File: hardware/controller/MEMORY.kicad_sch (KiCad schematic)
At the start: 8 parts, among them IC3 4677, IC4 W25Q256JVEIQ

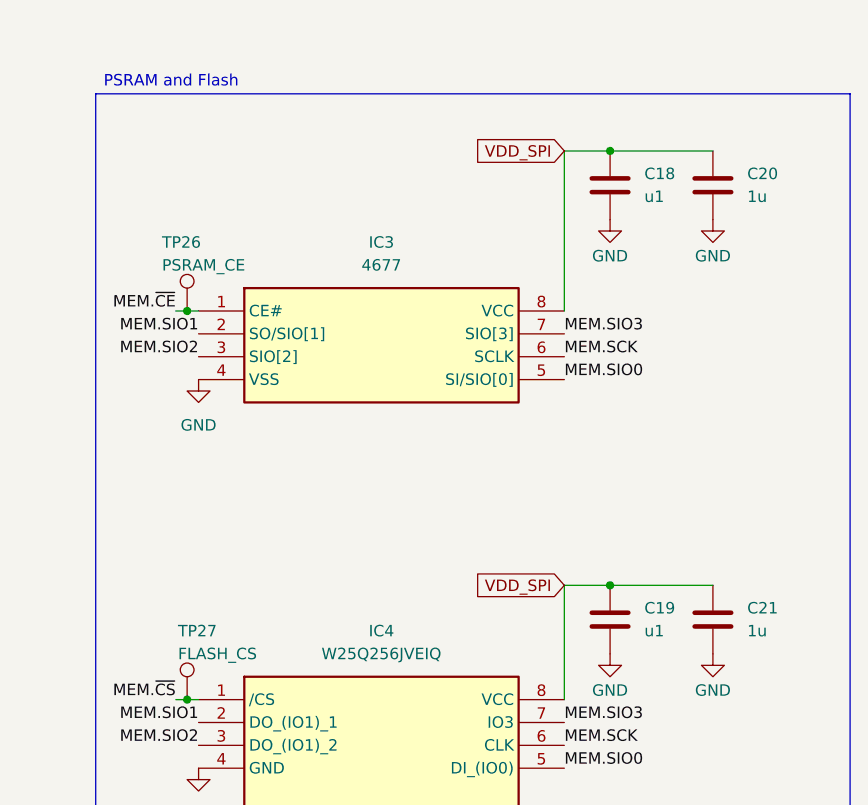
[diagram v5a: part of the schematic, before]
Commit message: ERC good to go. grouped all components on pcb
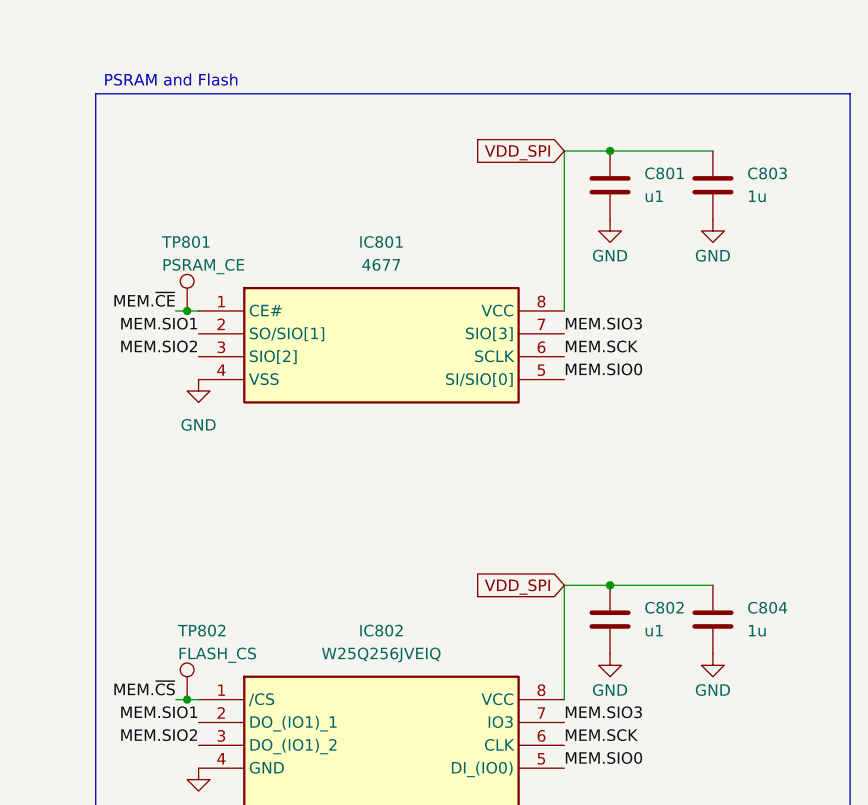
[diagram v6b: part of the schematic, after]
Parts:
- C801: renamed from C18; footprint MAJx16 -> SamacSys_Parts:MAJx16
- C802: renamed from C19; footprint MAJx16 -> SamacSys_Parts:MAJx16
- C803: renamed from C20; footprint CAPC2012X135N -> SamacSys_Parts:CAPC2012X135N
- C804: renamed from C21; footprint CAPC2012X135N -> SamacSys_Parts:CAPC2012X135N
- IC801: renamed from IC3; footprint SOIC127P600X175-8N -> SamacSys_Parts:SOIC127P600X175-8N
- IC802: renamed from IC4; footprint SON127P800X600X80-9N-D -> SamacSys_Parts:SON127P800X600X80-9N-D
- renumbered TP26 to TP801, TP27 to TP802
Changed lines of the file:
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@@
 		(dnp no)
 		(fields_autoplaced yes)
-		(property "Reference" "#PWR062"
+		(property "Reference" "#PWR0801"
 			(at 119.38 96.52 0)
 			(effects
@@
 			(project "controller"
 				(path "/869bea87-c885-4ead-826b-3f34ceacafad/0e7b3f4d-646f-4949-ba8d-4e4489aa7d1d"
-					(reference "#PWR062")
+					(reference "#PWR0801")
 					(unit 1)
 				)
@@
 		(dnp no)
 		(fields_autoplaced yes)
-		(property "Reference" "C19"
+		(property "Reference" "C802"
 			(at 168.91 115.5699 0)
 			(effects
@@
 			)
 		)
-		(property "Footprint" "MAJx16"
+		(property "Footprint" "SamacSys_Parts:MAJx16"
 			(at 173.99 213.03 0)
 			(effects
@@
 			(project "controller"
 				(path "/869bea87-c885-4ead-826b-3f34ceacafad/0e7b3f4d-646f-4949-ba8d-4e4489aa7d1d"
-					(reference "C19")
+					(reference "C802")
 					(unit 1)
 				)
@@
 		(dnp no)
 		(fields_autoplaced yes)
-		(property "Reference" "IC4"
+		(property "Reference" "IC802"
 			(at 139.7 118.11 0)
 			(effects
@@
 			)
 		)
-		(property "Footprint" "SON127P800X600X80-9N-D"
+		(property "Footprint" "SamacSys_Parts:SON127P800X600X80-9N-D"
 			(at 156.21 220.65 0)
 			(effects
@@
 			(project "controller"
 				(path "/869bea87-c885-4ead-826b-3f34ceacafad/0e7b3f4d-646f-4949-ba8d-4e4489aa7d1d"
-					(reference "IC4")
+					(reference "IC802")
 					(unit 1)
 				)
@@
 		(on_board yes)
 		(dnp no)
-		(property "Reference" "#PWR067"
+		(property "Reference" "#PWR0806"
 			(at 176.53 78.74 0)
 			(effects
@@
 			(project "controller"
 				(path "/869bea87-c885-4ead-826b-3f34ceacafad/0e7b3f4d-646f-4949-ba8d-4e4489aa7d1d"
-					(reference "#PWR067")
+					(reference "#PWR0806")
 					(unit 1)
 				)
@@
 		(dnp no)
 		(fields_autoplaced yes)
-		(property "Reference" "C20"
+		(property "Reference" "C803"
 			(at 180.34 67.3099 0)
 			(effects
@@
 			)
 		)
-		(property "Footprint" "CAPC2012X135N"
+		(property "Footprint" "SamacSys_Parts:CAPC2012X135N"
 			(at 185.42 164.77 0)
 			(effects
@@
 			(project "controller"
 				(path "/869bea87-c885-4ead-826b-3f34ceacafad/0e7b3f4d-646f-4949-ba8d-4e4489aa7d1d"
-					(reference "C20")
+					(reference "C803")
 					(unit 1)
 				)
@@
 		(dnp no)
 		(fields_autoplaced yes)
-		(property "Reference" "IC3"
+		(property "Reference" "IC801"
 			(at 139.7 74.93 0)
 			(effects
@@
 			)
 		)
-		(property "Footprint" "SOIC127P600X175-8N"
+		(property "Footprint" "SamacSys_Parts:SOIC127P600X175-8N"
 			(at 156.21 177.47 0)
 			(effects
@@
 			(project "controller"
 				(path "/869bea87-c885-4ead-826b-3f34ceacafad/0e7b3f4d-646f-4949-ba8d-4e4489aa7d1d"
-					(reference "IC3")
+					(reference "IC801")
 					(unit 1)
 				)
@@
 		(on_board yes)
 		(dnp no)
-		(property "Reference" "#PWR065"
+		(property "Reference" "#PWR0804"
 			(at 165.1 78.74 0)
 			(effects
@@
 			(project "controller"
 				(path "/869bea87-c885-4ead-826b-3f34ceacafad/0e7b3f4d-646f-4949-ba8d-4e4489aa7d1d"
-					(reference "#PWR065")
+					(reference "#PWR0804")
 					(unit 1)
 				)
@@
 		(dnp no)
 		(fields_autoplaced yes)
-		(property "Reference" "#PWR064"
+		(property "Reference" "#PWR0803"
 			(at 139.7 152.4 0)
 			(effects
@@
 			(project "controller"
 				(path "/869bea87-c885-4ead-826b-3f34ceacafad/0e7b3f4d-646f-4949-ba8d-4e4489aa7d1d"
-					(reference "#PWR064")
+					(reference "#PWR0803")
 					(unit 1)
 				)
@@
 		(on_board yes)
 		(dnp no)
-		(property "Reference" "#PWR068"
+		(property "Reference" "#PWR0807"
 			(at 176.53 127 0)
 			(effects
@@
 			(project "controller"
 				(path "/869bea87-c885-4ead-826b-3f34ceacafad/0e7b3f4d-646f-4949-ba8d-4e4489aa7d1d"
-					(reference "#PWR068")
+					(reference "#PWR0807")
 					(unit 1)
 				)
@@
 		(on_board yes)
 		(dnp no)
-		(property "Reference" "#PWR066"
+		(property "Reference" "#PWR0805"
 			(at 165.1 127 0)
 			(effects
@@
 			(project "controller"
 				(path "/869bea87-c885-4ead-826b-3f34ceacafad/0e7b3f4d-646f-4949-ba8d-4e4489aa7d1d"
-					(reference "#PWR066")
+					(reference "#PWR0805")
 					(unit 1)
 				)
@@
 		(on_board yes)
 		(dnp no)
-		(property "Reference" "TP27"
+		(property "Reference" "TP802"
 			(at 117.094 118.11 0)
 			(effects
@@
 			(project "controller"
 				(path "/869bea87-c885-4ead-826b-3f34ceacafad/0e7b3f4d-646f-4949-ba8d-4e4489aa7d1d"
-					(reference "TP27")
+					(reference "TP802")
 					(unit 1)
 				)
@@
 		(dnp no)
 		(fields_autoplaced yes)
-		(property "Reference" "#PWR063"
+		(property "Reference" "#PWR0802"
 			(at 119.38 139.7 0)
 			(effects
@@
 			(project "controller"
 				(path "/869bea87-c885-4ead-826b-3f34ceacafad/0e7b3f4d-646f-4949-ba8d-4e4489aa7d1d"
-					(reference "#PWR063")
+					(reference "#PWR0802")
 					(unit 1)
 				)
@@
 		(dnp no)
 		(fields_autoplaced yes)
-		(property "Reference" "C18"
+		(property "Reference" "C801"
 			(at 168.91 67.3099 0)
 			(effects
@@
 			)
 		)
-		(property "Footprint" "MAJx16"
+		(property "Footprint" "SamacSys_Parts:MAJx16"
 			(at 173.99 164.77 0)
 			(effects
@@
 			(project "controller"
 				(path "/869bea87-c885-4ead-826b-3f34ceacafad/0e7b3f4d-646f-4949-ba8d-4e4489aa7d1d"
-					(reference "C18")
+					(reference "C801")
 					(unit 1)
 				)
@@
 		(on_board yes)
 		(dnp no)
-		(property "Reference" "TP26"
+		(property "Reference" "TP801"
 			(at 115.316 74.93 0)
 			(effects
@@
 			(project "controller"
 				(path "/869bea87-c885-4ead-826b-3f34ceacafad/0e7b3f4d-646f-4949-ba8d-4e4489aa7d1d"
-					(reference "TP26")
+					(reference "TP801")
 					(unit 1)
 				)
@@
 		(dnp no)
 		(fields_autoplaced yes)
-		(property "Reference" "C21"
+		(property "Reference" "C804"
 			(at 180.34 115.5699 0)
 			(effects
@@
 			)
 		)
-		(property "Footprint" "CAPC2012X135N"
+		(property "Footprint" "SamacSys_Parts:CAPC2012X135N"
 			(at 185.42 213.03 0)
 			(effects
@@
 			(project "controller"
 				(path "/869bea87-c885-4ead-826b-3f34ceacafad/0e7b3f4d-646f-4949-ba8d-4e4489aa7d1d"
-					(reference "C21")
-					(unit 1)
-				)
+					(reference "C804")
+					(unit 1)
+				)

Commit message: save before nuke
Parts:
- renumbered C801 to C119, C802 to C120, C803 to C121, C804 to C122, IC801 to IC103, IC802 to IC104, TP801 to TP126, TP802 to TP127
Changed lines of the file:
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@@
 		(dnp no)
 		(fields_autoplaced yes)
-		(property "Reference" "#PWR0801"
+		(property "Reference" "#PWR0163"
 			(at 119.38 96.52 0)
 			(effects
@@
 			(project "controller"
 				(path "/869bea87-c885-4ead-826b-3f34ceacafad/0e7b3f4d-646f-4949-ba8d-4e4489aa7d1d"
-					(reference "#PWR0801")
+					(reference "#PWR0163")
 					(unit 1)
 				)
@@
 		(dnp no)
 		(fields_autoplaced yes)
-		(property "Reference" "C802"
+		(property "Reference" "C120"
 			(at 168.91 115.5699 0)
 			(effects
@@
 			(project "controller"
 				(path "/869bea87-c885-4ead-826b-3f34ceacafad/0e7b3f4d-646f-4949-ba8d-4e4489aa7d1d"
-					(reference "C802")
+					(reference "C120")
 					(unit 1)
 				)
@@
 		(dnp no)
 		(fields_autoplaced yes)
-		(property "Reference" "IC802"
+		(property "Reference" "IC104"
 			(at 139.7 118.11 0)
 			(effects
@@
 			(project "controller"
 				(path "/869bea87-c885-4ead-826b-3f34ceacafad/0e7b3f4d-646f-4949-ba8d-4e4489aa7d1d"
-					(reference "IC802")
+					(reference "IC104")
 					(unit 1)
 				)
@@
 		(on_board yes)
 		(dnp no)
-		(property "Reference" "#PWR0806"
+		(property "Reference" "#PWR0168"
 			(at 176.53 78.74 0)
 			(effects
@@
 			(project "controller"
 				(path "/869bea87-c885-4ead-826b-3f34ceacafad/0e7b3f4d-646f-4949-ba8d-4e4489aa7d1d"
-					(reference "#PWR0806")
+					(reference "#PWR0168")
 					(unit 1)
 				)
@@
 		(dnp no)
 		(fields_autoplaced yes)
-		(property "Reference" "C803"
+		(property "Reference" "C121"
 			(at 180.34 67.3099 0)
 			(effects
@@
 			(project "controller"
 				(path "/869bea87-c885-4ead-826b-3f34ceacafad/0e7b3f4d-646f-4949-ba8d-4e4489aa7d1d"
-					(reference "C803")
+					(reference "C121")
 					(unit 1)
 				)
@@
 		(dnp no)
 		(fields_autoplaced yes)
-		(property "Reference" "IC801"
+		(property "Reference" "IC103"
 			(at 139.7 74.93 0)
 			(effects
@@
 			(project "controller"
 				(path "/869bea87-c885-4ead-826b-3f34ceacafad/0e7b3f4d-646f-4949-ba8d-4e4489aa7d1d"
-					(reference "IC801")
+					(reference "IC103")
 					(unit 1)
 				)
@@
 		(on_board yes)
 		(dnp no)
-		(property "Reference" "#PWR0804"
+		(property "Reference" "#PWR0166"
 			(at 165.1 78.74 0)
 			(effects
@@
 			(project "controller"
 				(path "/869bea87-c885-4ead-826b-3f34ceacafad/0e7b3f4d-646f-4949-ba8d-4e4489aa7d1d"
-					(reference "#PWR0804")
+					(reference "#PWR0166")
 					(unit 1)
 				)
@@
 		(dnp no)
 		(fields_autoplaced yes)
-		(property "Reference" "#PWR0803"
+		(property "Reference" "#PWR0165"
 			(at 139.7 152.4 0)
 			(effects
@@
 			(project "controller"
 				(path "/869bea87-c885-4ead-826b-3f34ceacafad/0e7b3f4d-646f-4949-ba8d-4e4489aa7d1d"
-					(reference "#PWR0803")
+					(reference "#PWR0165")
 					(unit 1)
 				)
@@
 		(on_board yes)
 		(dnp no)
-		(property "Reference" "#PWR0807"
+		(property "Reference" "#PWR0169"
 			(at 176.53 127 0)
 			(effects
@@
 			(project "controller"
 				(path "/869bea87-c885-4ead-826b-3f34ceacafad/0e7b3f4d-646f-4949-ba8d-4e4489aa7d1d"
-					(reference "#PWR0807")
+					(reference "#PWR0169")
 					(unit 1)
 				)
@@
 		(on_board yes)
 		(dnp no)
-		(property "Reference" "#PWR0805"
+		(property "Reference" "#PWR0167"
 			(at 165.1 127 0)
 			(effects
@@
 			(project "controller"
 				(path "/869bea87-c885-4ead-826b-3f34ceacafad/0e7b3f4d-646f-4949-ba8d-4e4489aa7d1d"
-					(reference "#PWR0805")
+					(reference "#PWR0167")
 					(unit 1)
 				)
@@
 		(on_board yes)
 		(dnp no)
-		(property "Reference" "TP802"
+		(property "Reference" "TP127"
 			(at 117.094 118.11 0)
 			(effects
@@
 			(project "controller"
 				(path "/869bea87-c885-4ead-826b-3f34ceacafad/0e7b3f4d-646f-4949-ba8d-4e4489aa7d1d"
-					(reference "TP802")
+					(reference "TP127")
 					(unit 1)
 				)
@@
 		(dnp no)
 		(fields_autoplaced yes)
-		(property "Reference" "#PWR0802"
+		(property "Reference" "#PWR0164"
 			(at 119.38 139.7 0)
 			(effects
@@
 			(project "controller"
 				(path "/869bea87-c885-4ead-826b-3f34ceacafad/0e7b3f4d-646f-4949-ba8d-4e4489aa7d1d"
-					(reference "#PWR0802")
+					(reference "#PWR0164")
 					(unit 1)
 				)
@@
 		(dnp no)
 		(fields_autoplaced yes)
-		(property "Reference" "C801"
+		(property "Reference" "C119"
 			(at 168.91 67.3099 0)
 			(effects
@@
 			(project "controller"
 				(path "/869bea87-c885-4ead-826b-3f34ceacafad/0e7b3f4d-646f-4949-ba8d-4e4489aa7d1d"
-					(reference "C801")
+					(reference "C119")
 					(unit 1)
 				)
@@
 		(on_board yes)
 		(dnp no)
-		(property "Reference" "TP801"
+		(property "Reference" "TP126"
 			(at 115.316 74.93 0)
 			(effects
@@
 			(project "controller"
 				(path "/869bea87-c885-4ead-826b-3f34ceacafad/0e7b3f4d-646f-4949-ba8d-4e4489aa7d1d"
-					(reference "TP801")
+					(reference "TP126")
 					(unit 1)
 				)
@@
 		(dnp no)
 		(fields_autoplaced yes)
-		(property "Reference" "C804"
+		(property "Reference" "C122"
 			(at 180.34 115.5699 0)
 			(effects
@@
 			(project "controller"
 				(path "/869bea87-c885-4ead-826b-3f34ceacafad/0e7b3f4d-646f-4949-ba8d-4e4489aa7d1d"
-					(reference "C804")
-					(unit 1)
-				)
+					(reference "C122")
+					(unit 1)
+				)
